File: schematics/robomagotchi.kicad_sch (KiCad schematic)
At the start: 23 parts

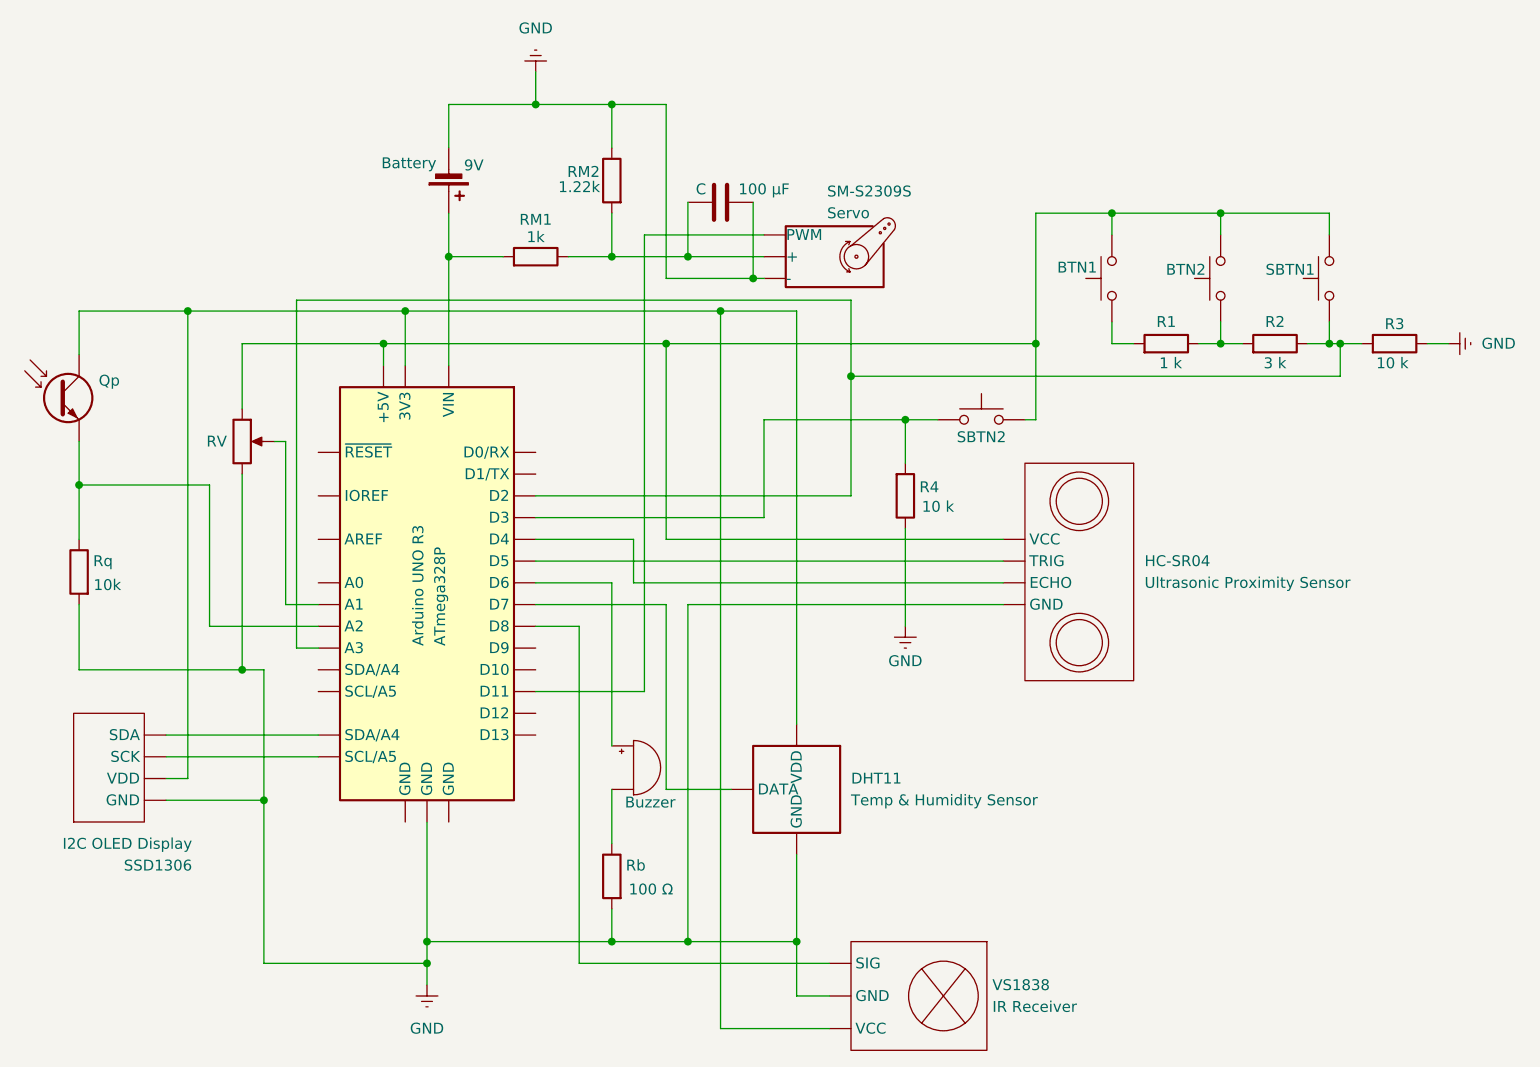
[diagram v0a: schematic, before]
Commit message: Replaced FEEDING state with SINGING state
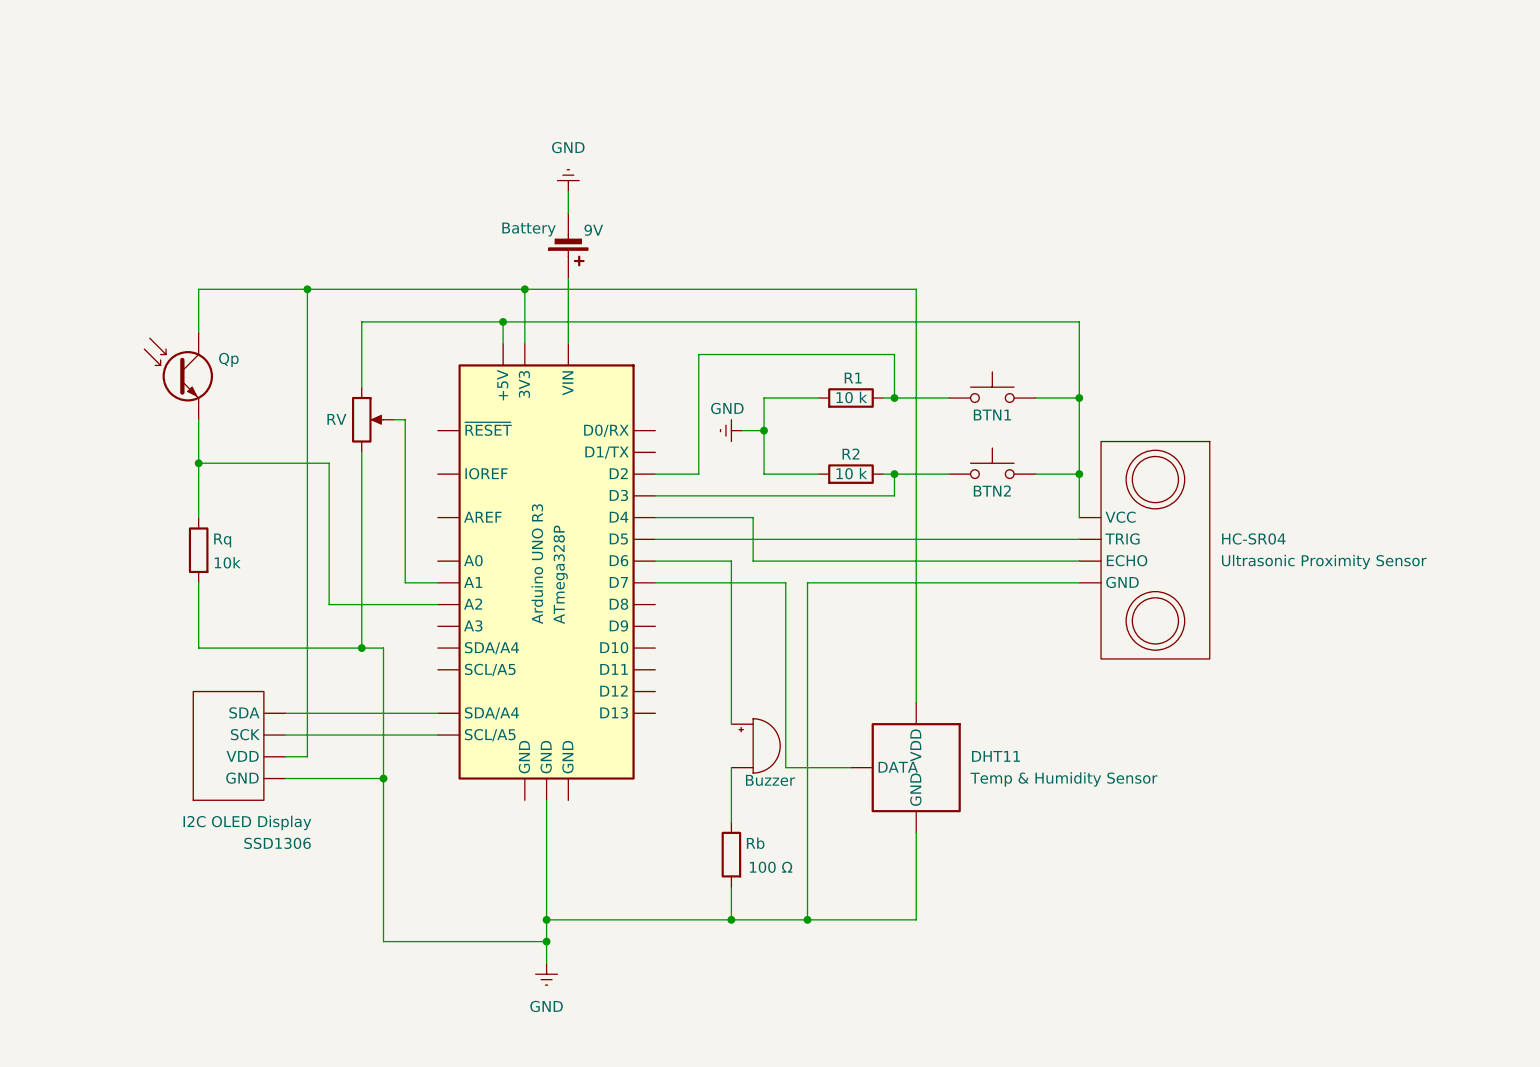
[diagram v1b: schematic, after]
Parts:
- removed C: 100 μF, symbol Device:C
- removed R1: 1 k, symbol Device:R
- removed R2: 3 k, symbol Device:R
- removed RM1: 1k, symbol Device:R
- removed RM2: 1.22k, symbol Device:R
- removed SBTN1: SW_Push, symbol Switch:SW_Push
- removed SBTN_A: BTN2, symbol Switch:SW_Push
- removed SM-S2309S: Servo, symbol Motor:Motor_Servo
- removed VS1838: IR Receiver, symbol My_Symbols:VS1838B_IR_RECEIVER
- renumbered SBTN2 to BTN2, R4 to R1, R3 to R2
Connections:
- net GND: now also R1.2, R2.2; no longer R1.1, R2.1
- net at ATmega328P.18 (D3), BTN2.1: now also R2.1; no longer R1.2
- net at BTN1.1: now also ATmega328P.17 (D2), R1.1
- now unconnected: ATmega328P.12 (A3)
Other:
- moved on the sheet: ATmega328P, BTN2, Battery, DHT11, HC-SR04, Qp, R1, R2, RV, Rb, Rq, SSD1306
